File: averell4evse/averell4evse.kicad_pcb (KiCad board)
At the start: 2 copper layers, 91 x 78 mm, 43 parts, among them J1 Conn_01x16, J2 CONNFLY_Elec_DS1129-04-S8B0P-X, J3 Conn_01x04, J4 Conn_01x03, J5 Conn_01x09, U1 KT2520K-T, U2 NFCv4, U3 TLC5957RTQ, U4 74AUC2G125, U5 touch_sensor

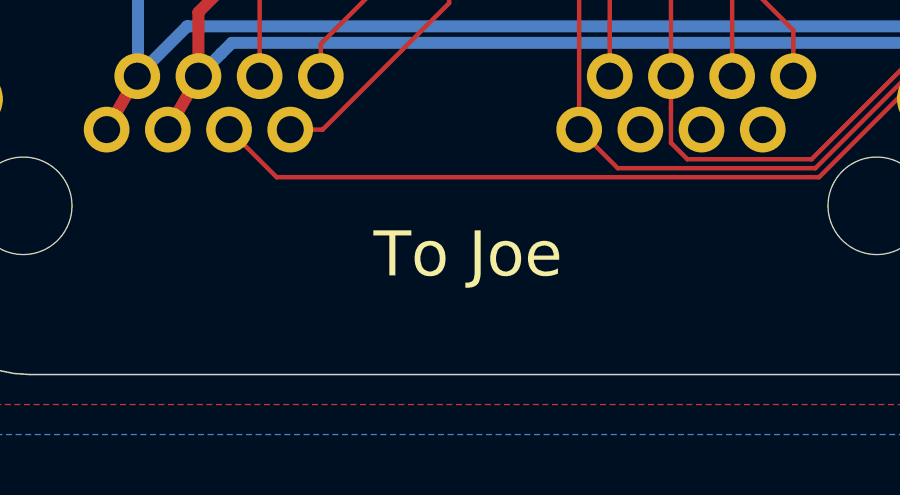
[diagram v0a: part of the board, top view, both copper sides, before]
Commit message: averell/pcb: Add silk with RJ45 numbering
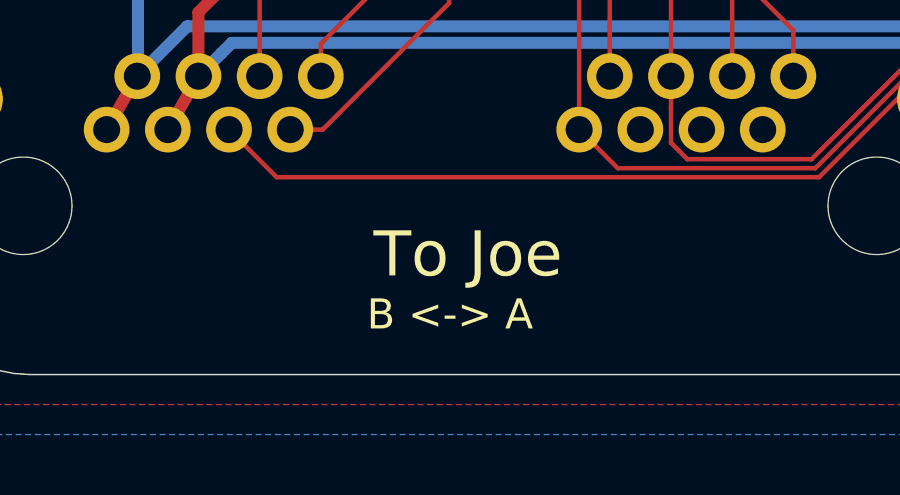
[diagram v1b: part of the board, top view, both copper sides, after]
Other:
- board text added: "A <-> B"
- board text added: "B <-> A"
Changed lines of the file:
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@@
-(kicad_pcb (version 20171130) (host pcbnew "(5.1.0)-1")
+(kicad_pcb (version 20171130) (host pcbnew "(5.1.5)-2")
   (general
     (thickness 1.6)
-    (drawings 33)
+    (drawings 35)
     (tracks 1144)
     (zones 0)
@@
   )
   (setup
-    (last_trace_width 0.4)
+    (last_trace_width 0.15)
     (user_trace_width 0.15)
     (user_trace_width 0.25)
@@
   (module ma4evse:CONNFLY_Elec_DS1129-04-S8B0P-X (layer B.Cu)
     (at 93 121 180)
-    (fp_text reference J2 (at -10.23 8.86 180) (layer B.SilkS)
+    (fp_text reference J2 (at -18 7 180) (layer B.SilkS)
       (effects (font (size 1 1) (thickness 0.15)) (justify mirror))
     )
@@
     )
   )
+  (gr_text "A <-> B" (at 98.5 112.25) (layer B.SilkS)
+    (effects (font (size 1 1) (thickness 0.15)) (justify mirror))
+  )
+  (gr_text "B <-> A" (at 93 127) (layer F.SilkS)
+    (effects (font (size 1 1) (thickness 0.15)))
+  )
   (gr_text SIGIN (at 138 68 270) (layer B.SilkS)
     (effects (font (size 1 1) (thickness 0.15)) (justify left mirror))
@@
     (effects (font (size 1.5 1.5) (thickness 0.3)) (justify mirror))
   )
-  (gr_text "To Joe" (at 90 111.8) (layer B.SilkS)
+  (gr_text "To Joe" (at 90 110) (layer B.SilkS)
     (effects (font (size 1.5 1.5) (thickness 0.3)) (justify mirror))
   )
@@
   (segment (start 120.400001 107.325001) (end 125.052001 107.325001) (width 0.15) (layer B.Cu) (net 45))
   (via (at 88.5 111.4) (size 0.6) (drill 0.3) (layers F.Cu B.Cu) (net 45))
-  (segment (start 93.5 114.1) (end 94.2 114.8) (width 0.15) (layer B.Cu) (net 81))
   (segment (start 100.365 116.025682) (end 96.849298 112.50998) (width 0.15) (layer F.Cu) (net 45))
   (segment (start 100.365 119.055) (end 100.365 116.025682) (width 0.15) (layer F.Cu) (net 45))
@@
   (segment (start 125.3 106.3) (end 124.899992 105.899992) (width 0.15) (layer F.Cu) (net 78))
   (segment (start 124.899992 105.899992) (end 119.823007 105.899991) (width 0.15) (layer F.Cu) (net 78))
+  (segment (start 93.5 114.1) (end 94.2 114.8) (width 0.15) (layer B.Cu) (net 81))
   (zone (net 1) (net_name GND) (layer F.Cu) (hatch edge 0.508)
     (connect_pads (clearance 0.15))

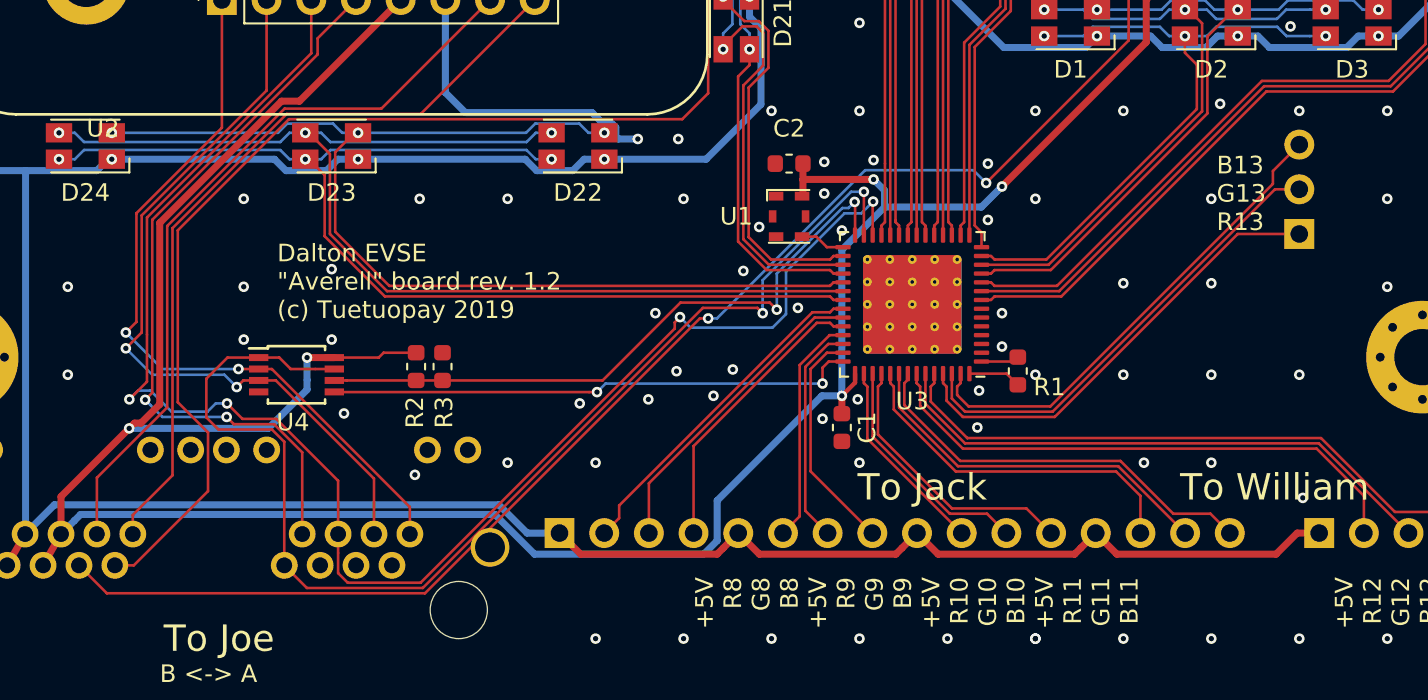
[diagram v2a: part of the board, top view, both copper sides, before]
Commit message: averell{sch, pcb}: Change oscillator and fix improper traces
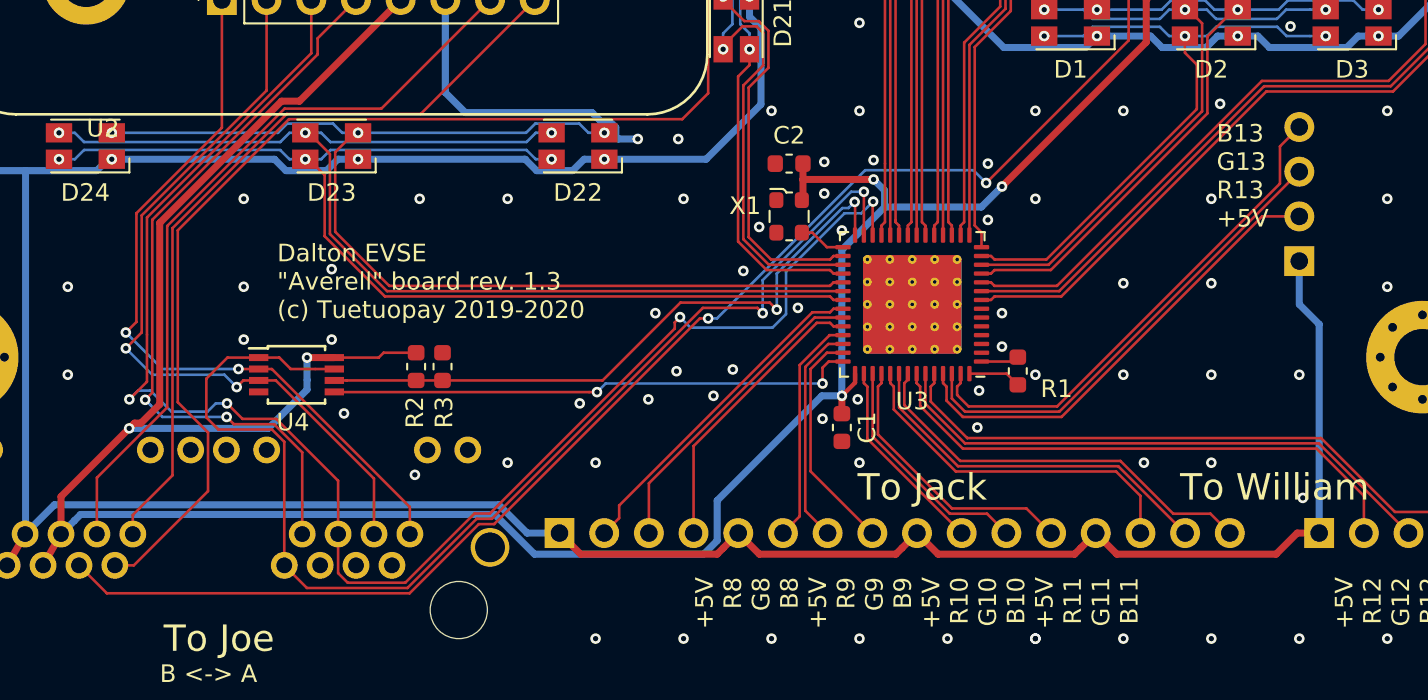
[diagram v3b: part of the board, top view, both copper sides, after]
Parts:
- removed U1: KT2520K-T, Oscillator:Oscillator_SMD_Kyocera_2520-6Pin_2.5x2.0mm
- added X1: ECS-2520MV-xxx-xx, Oscillator:Oscillator_SMD_ECS_2520MV-xxx-xx-4Pin_2.5x2.0mm, F.Cu at (126.0, 101.0)
- J4: value Conn_01x03 -> Conn_01x04; footprint Connector_PinHeader_2.54mm:PinHeader_1x03_P2.54mm_Horizontal -> Connector_PinHeader_2.54mm:PinHeader_1x04_P2.54mm_Horizontal
- moved J4 1.54 mm to (155.0, 103.5)
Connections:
- J4 pad 1: Net-(J4-Pad1) -> +5V
- U3 pad 53: Net-(J4-Pad1) -> Net-(J4-Pad2)
- U3 pad 54: Net-(J4-Pad2) -> Net-(J4-Pad3)
- U3 pad 55: Net-(J4-Pad3) -> Net-(J4-Pad4)
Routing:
- net Net-(J4-Pad4): track 0.00 -> 28.8 mm
- net Net-(J4-Pad1): track 26.4 -> 0.00 mm
- net +5V: track 381.3 -> 397.2 mm
- net GND: vias 87 -> 86
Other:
- board text added: "B13 G13 R13 +5V"
- board text added: "Dalton EVSE "Averell" board rev. 1.3 (c) Tuetuopay 2019-2020"
- board text removed: "B13 G13 R13"
- board text removed: "Dalton EVSE "Averell" board rev. 1.2 (c) Tuetuopay 2019"

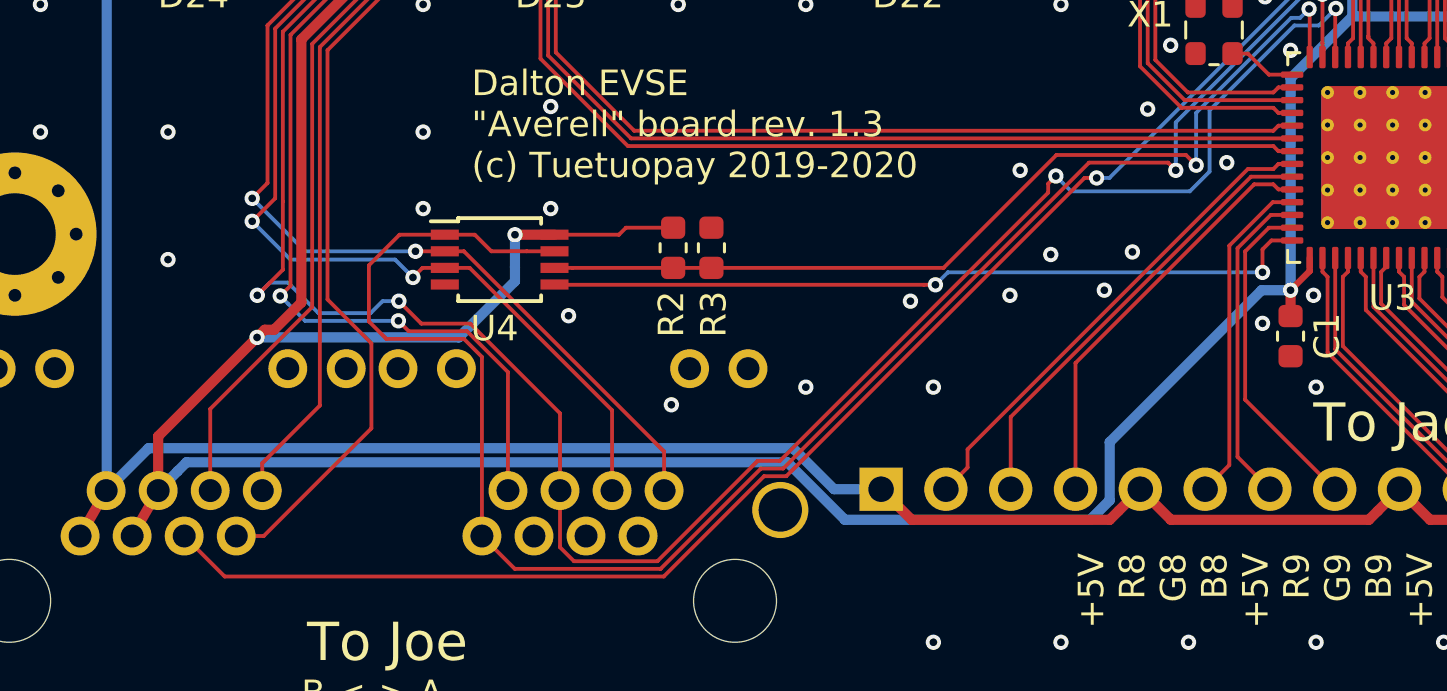
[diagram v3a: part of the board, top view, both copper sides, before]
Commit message: averell/*: Remove LED driver CS thingy
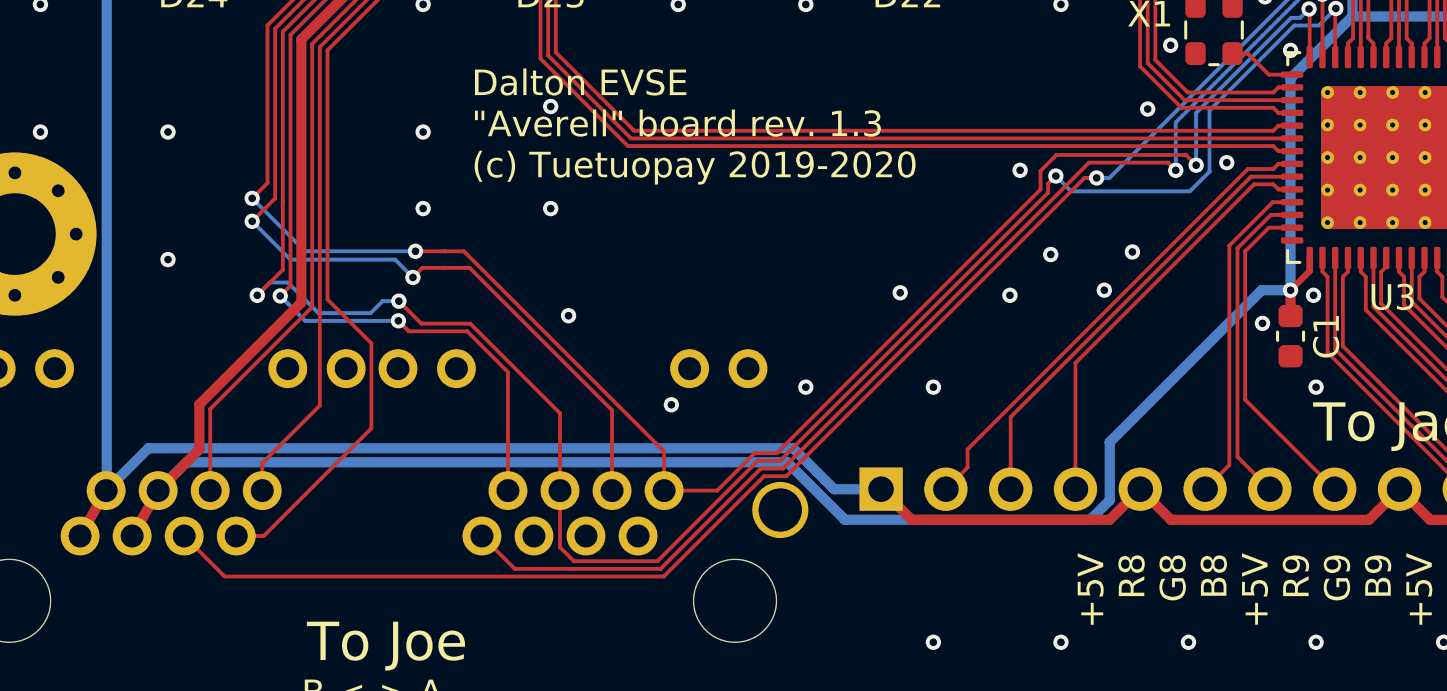
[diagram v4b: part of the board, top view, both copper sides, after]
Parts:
- removed R2, R3: 10k, Resistor_SMD:R_0603_1608Metric
- removed U4: 74AUC2G125, Package_SO:TSSOP-8_3x3mm_P0.65mm
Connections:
- net /DRV_CS renamed /DRV_LAT
- U3 pad 28: /DRV_SCK -> /SCK
- U3 pad 42: /LED_MISO -> Net-(U3-Pad42)
- X1 pad 1: Net-(X1-Pad1) -> (no net)
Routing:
- net /DRV_SCK: track 37.2 -> 0.00 mm, vias 2 -> 0
- net /SCK: track 43.0 -> 79.9 mm, vias 2 -> 4
- net /LED_MISO: track 30.2 -> 0.00 mm, vias 2 -> 0
- net /DRV_LAT: track 68.9 -> 46.6 mm
- net +3V3: track 183.7 -> 164.3 mm, vias 5 -> 3
